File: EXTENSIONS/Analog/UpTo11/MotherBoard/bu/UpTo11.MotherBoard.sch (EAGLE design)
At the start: 9 parts, among them X1 USB-A

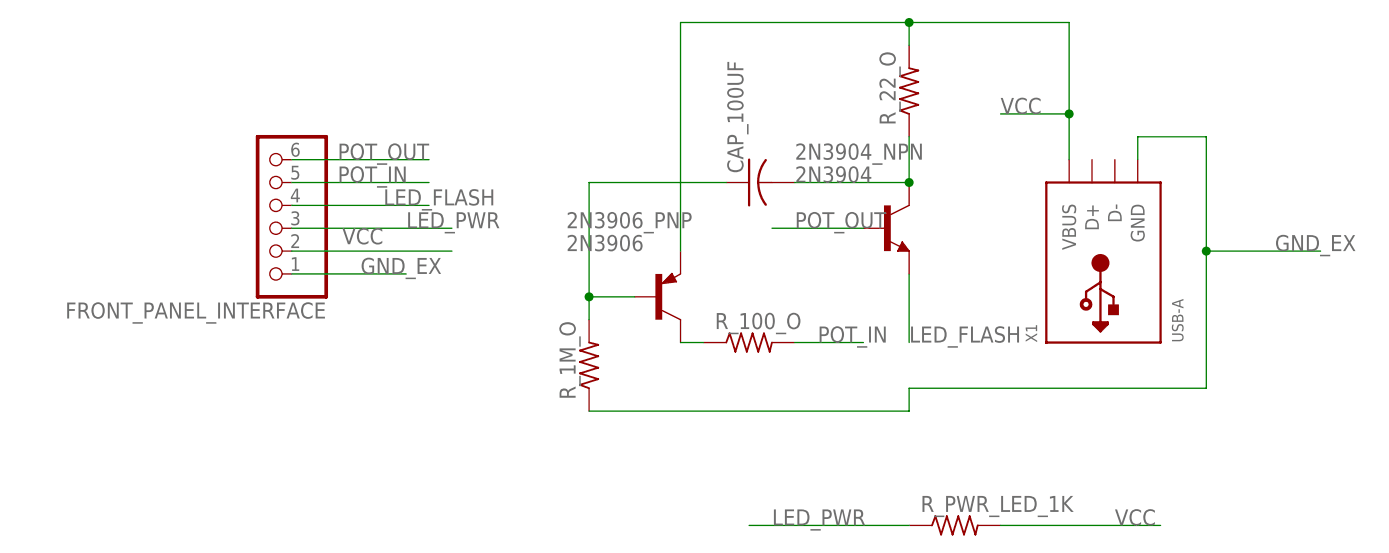
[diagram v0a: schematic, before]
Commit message: Create UpTo11 Front Panel
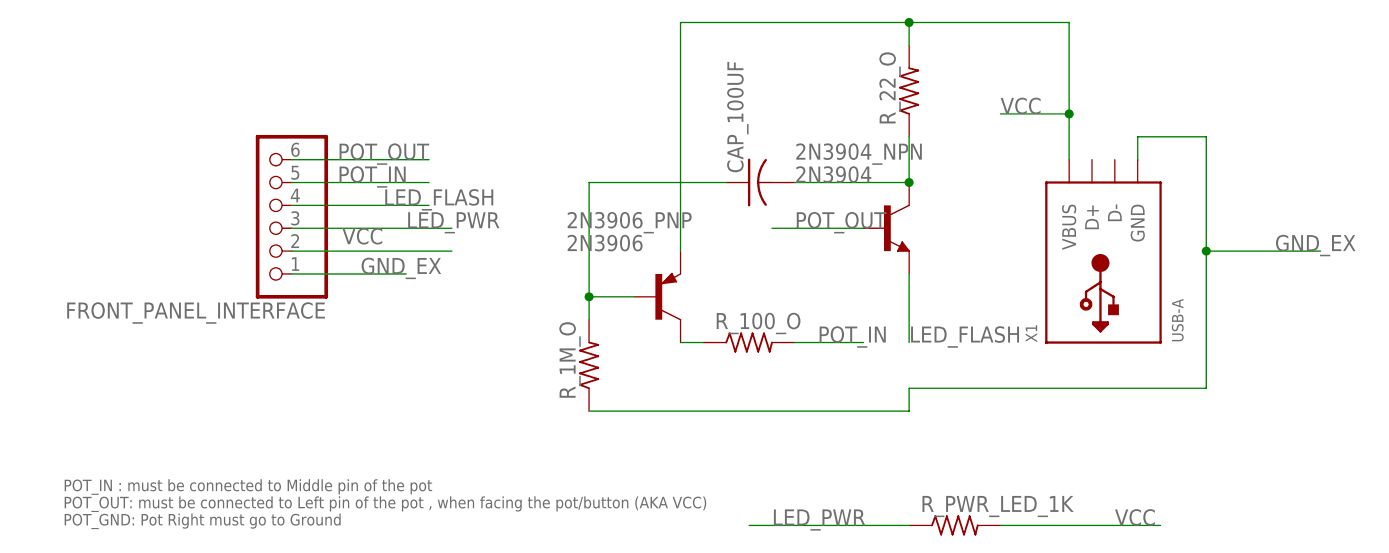
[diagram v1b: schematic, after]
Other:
- note added: "POT_IN : must be connected to Middle pin of the pot POT_OUT: must be connected to Left pin of the pot , when facing the pot/button (AKA VCC) POT_GND: Pot Right must go to Ground"
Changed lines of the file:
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@@
 <sheet>
 <plain>
+<text x="-25.4" y="45.72" size="1.27" layer="95">POT_IN : must be connected to Middle pin of the pot
+POT_OUT: must be connected to Left pin of the pot , when facing the pot/button (AKA VCC)
+POT_GND: Pot Right must go to Ground</text>
 </plain>
 <instances>
@@
 </schematic>
 </drawing>
+<compatibility>
+<note version="6.3" minversion="6.2.2" severity="warning">
+Since Version 6.2.2 text objects can contain more than one line,
+which will not be processed correctly with this version.
+</note>
+</compatibility>
 </eagle>

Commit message: Create UpTo11 Front Panel
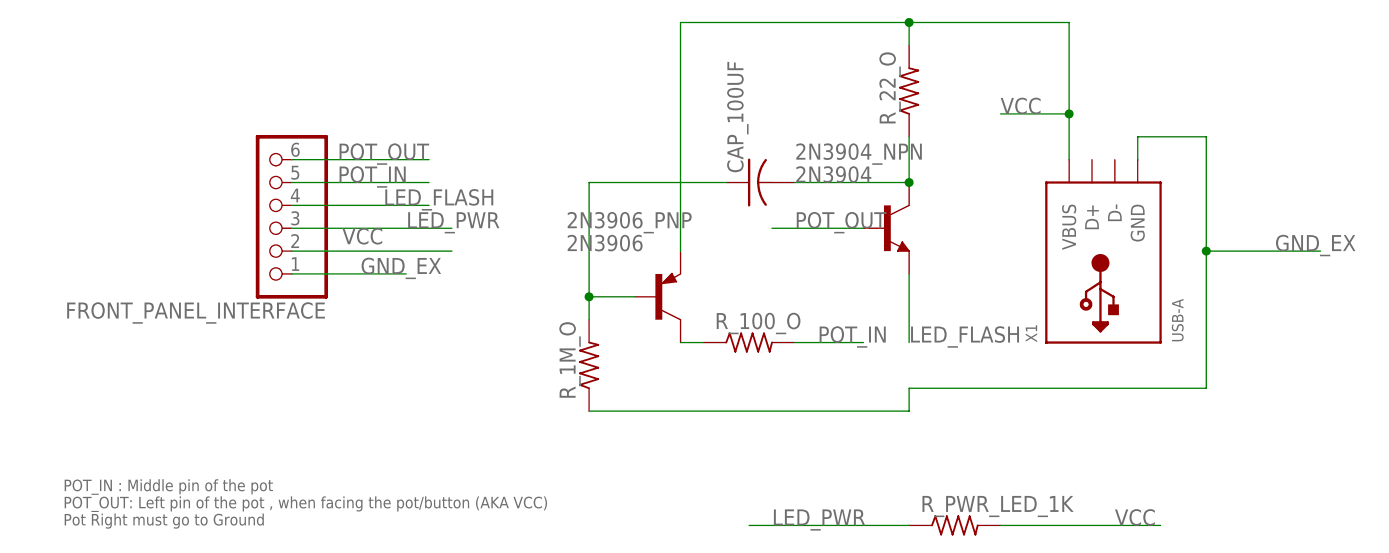
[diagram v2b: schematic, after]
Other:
- note added: "POT_IN : Middle pin of the pot POT_OUT: Left pin of the pot , when facing the pot/button (AKA VCC) Pot Right must go to Ground"
- note removed: "POT_IN : must be connected to Middle pin of the pot POT_OUT: must be connected to Left pin of the pot , when facing the pot/button (AKA VCC) POT_GND: Pot Right must go to Ground"
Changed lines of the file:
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@@
 <sheet>
 <plain>
-<text x="-25.4" y="45.72" size="1.27" layer="95">POT_IN : must be connected to Middle pin of the pot
-POT_OUT: must be connected to Left pin of the pot , when facing the pot/button (AKA VCC)
-POT_GND: Pot Right must go to Ground</text>
+<text x="-25.4" y="45.72" size="1.27" layer="95">POT_IN : Middle pin of the pot
+POT_OUT: Left pin of the pot , when facing the pot/button (AKA VCC)
+Pot Right must go to Ground</text>
 </plain>
 <instances>
